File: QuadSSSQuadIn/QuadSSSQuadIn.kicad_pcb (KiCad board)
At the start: 2 copper layers, 65 x 56 mm, 17 parts, among them IC1 ASSR-4128, IC2 ASSR-4128, J0 RPi_GPIO, J1 CONN_3X2, T1 CONN_8, T2 CONN_5, U1 MCP23008, U2 74AHC132

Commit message: Completed PC Board
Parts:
- added ?: , DWSLogoBCU, F.Cu at (95.1, 79.0)
- J1: value CONN_3X2 -> Address
- T1: value CONN_8 -> outputs
- T2: value CONN_5 -> Inputs
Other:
- board text added: "QuadSSSQuadIn (I2c) Copyright 2017 Deepwoods Software"

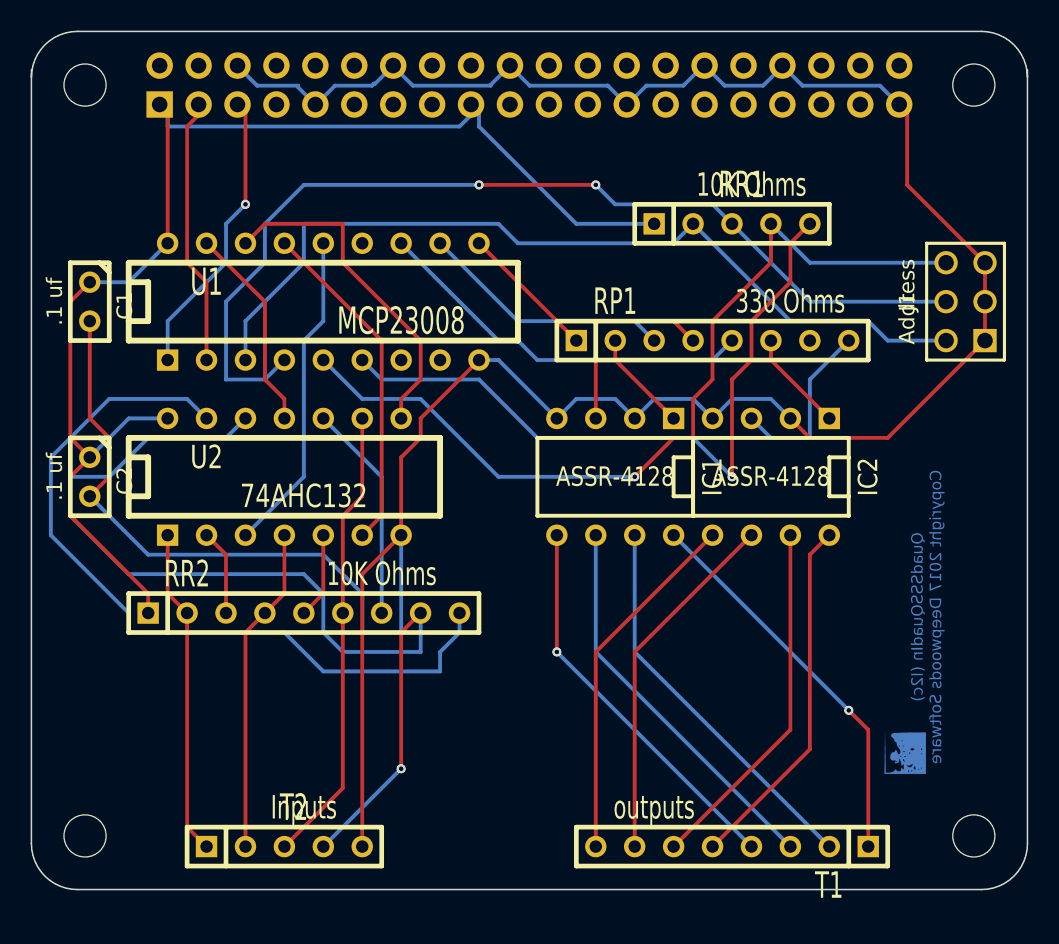
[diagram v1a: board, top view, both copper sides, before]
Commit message: Update QuadSSSQuadIn to use 5V logic input buffer (74lv125a)
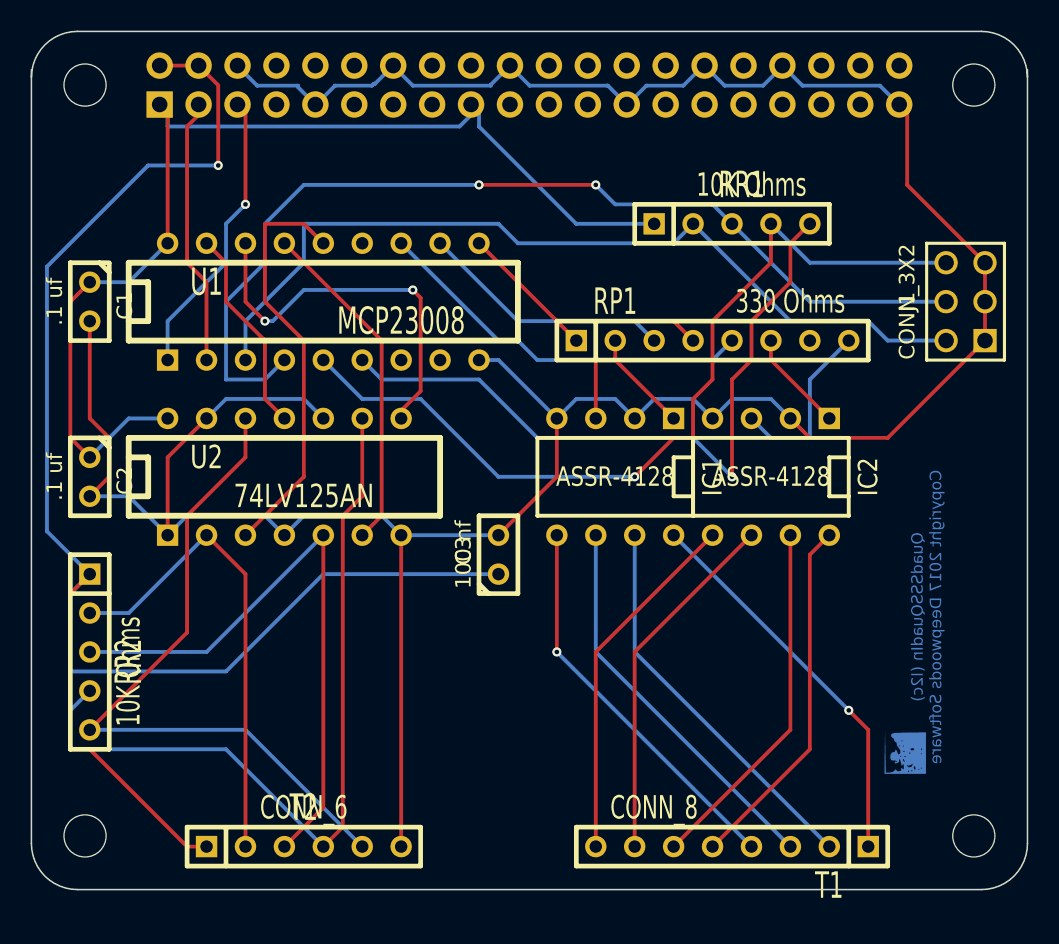
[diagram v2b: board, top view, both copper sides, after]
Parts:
- added C3: 100 nf, C1, F.Cu at (68.6, 66.0)
- J1: value Address -> CONN_3X2
- RR2: footprint SIL-9 -> SIL-5
- T1: value outputs -> CONN_8
- T2: value Inputs -> CONN_6; footprint SIL-5 -> SIL-6
- U2: value 74AHC132 -> 74LV125AN
- moved RR2 14.5 mm to (41.9, 73.7), turned to 270 degrees
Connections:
- J0 pad 2: (no net) -> +5V
- J0 pad 4: (no net) -> +5V
- RR2 pad 1: VDD -> +5V
- RR2 pad 2: N-0000024 (its old number) -> N-000007
- RR2 pad 3: N-000001 -> N-0000017
- RR2 pad 4: N-0000023 (its old number) -> N-0000020
- RR2 pad 5: N-000005 (its old number) -> N-0000019
- T2 pad 1: N-0000024 (its old number) -> +5V
- T2 pad 2: N-0000023 (its old number) -> N-000007
- T2 pad 3: N-0000014 (its old number) -> N-0000017
- T2 pad 4: N-0000013 (its old number) -> N-0000020
- T2 pad 5: GND -> N-0000019
- U2 pad 1: N-0000024 (its old number) -> GND
- U2 pad 10: N-000004 (its old number) -> GND
- U2 pad 12: N-0000013 (its old number) -> N-0000019
- U2 pad 13: N-000003 -> GND
- U2 pad 2: N-000001 -> N-000007
- U2 pad 4: N-0000023 (its old number) -> GND
- U2 pad 5: N-000005 (its old number) -> N-0000017
- U2 pad 9: N-0000014 (its old number) -> N-0000020
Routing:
- net +5V: track 0.00 -> 105.6 mm, vias 0 -> 1
- net N-0000013 (its old number): track 64.0 -> 0.00 mm, vias 1 -> 0
- net N-0000020: track 0.00 -> 52.5 mm
- net N-000003: track 51.5 -> 0.00 mm
- net N-0000019: track 0.00 -> 45.5 mm
- net N-0000017: track 0.00 -> 39.8 mm
- net N-000007: track 0.00 -> 31.1 mm
- net N-0000014 (its old number): track 30.0 -> 0.00 mm
- net N-0000024 (its old number): track 21.4 -> 0.00 mm
- net N-0000023 (its old number): track 21.4 -> 0.00 mm
- net N-000004 (its old number): track 14.3 -> 0.00 mm
- net VDD: track 86.1 -> 73.3 mm
- net GND: track 188.8 -> 198.7 mm
- net N-0000024: track 21.2 -> 27.3 mm
- net N-000005 (its old number): track 5.61 -> 0.00 mm
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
